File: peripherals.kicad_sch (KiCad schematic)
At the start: 14 parts, among them J2 GPS_ANT, U5 BME280, U6 LSM303AGR, U7 MAX-M10S, U8 RAK4630

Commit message: UPDATE RAK4630
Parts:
- added C39: 100n, symbol Device:C
- added C40: 10u, symbol Device:C
- added C41: 100N, symbol Device:C
- added J3: Conn_01x06, symbol Connector_Generic:Conn_01x06
- added J6: RF_LORA, symbol Connector:Conn_Coaxial
- added J7: BLE_ANT, symbol Connector:Conn_Coaxial
- added R25: 10K, symbol Device:R
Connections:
- net +3.3V: now also U8.40 (VBAT_IO_SX), U8.42 (VBAT_SX), C39.1, C40.1; no longer C35.2, C38.1, U5.6 (VDDIO), U6.10 (VDD_IO)
- net GND: now also U7.15 (VIO_SEL), U8.1 (GND), U8.2 (GND1), U8.3 (GND2), U8.4 (GND3), U8.5 (GND4), U8.6 (GND5), U8.7 (GND6), C39.2, C40.2, C41.2, J3.3 (Pin_3), J3.6 (Pin_6), J6.2 (Ext), J7.2 (Ext)
- net VSYS: now also U8.41 (VBAT_NRF)
- net at U8.34 (RF_BT): now also J7.1 (In)
- net at U8.35 (RF_LORA): now also J6.1 (In)
- net SWDCLK: now reaches U8.36 (SWDCLK)
- net SWDCLK: now also J3.4 (Pin_4)
- net SWDIO: now reaches U8.37 (SWDIO)
- net SWDIO: now also J3.2 (Pin_2)
- net VBUS: now reaches U8.43 (VBUS)
- net LORA_VDD: now reaches U8.44 (VDD_NRF)
- net LORA_VDD: now also J3.1 (Pin_1), R25.1
- net NRF_RST: now reaches U8.8 (NRF_RESET)
- net NRF_RST: now also C41.1, J3.5 (Pin_5), R25.2
- new net +1.8V: C35.2, C38.1, U5.6 (VDDIO), U6.10 (VDD_IO)
- no-connect marks 13 -> 12
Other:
- moved on the sheet: LoRa1, LoRa_PWR1, RCC1, U8, VSYS1

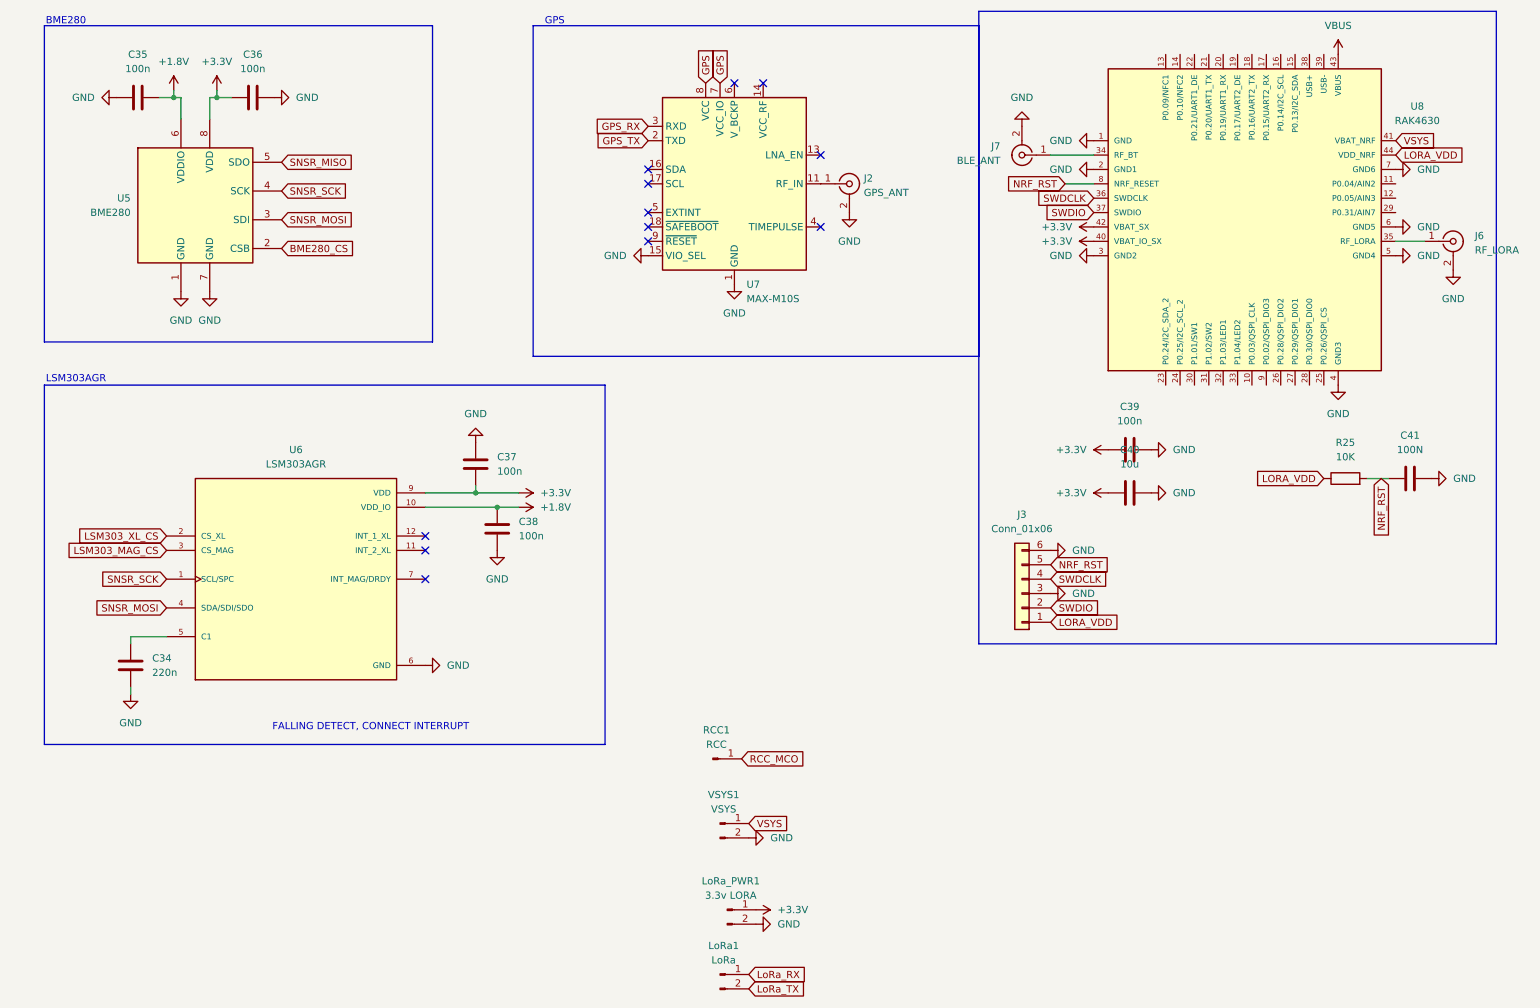
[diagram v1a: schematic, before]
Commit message: Modified lora module design, still need led and usb connected for flashing
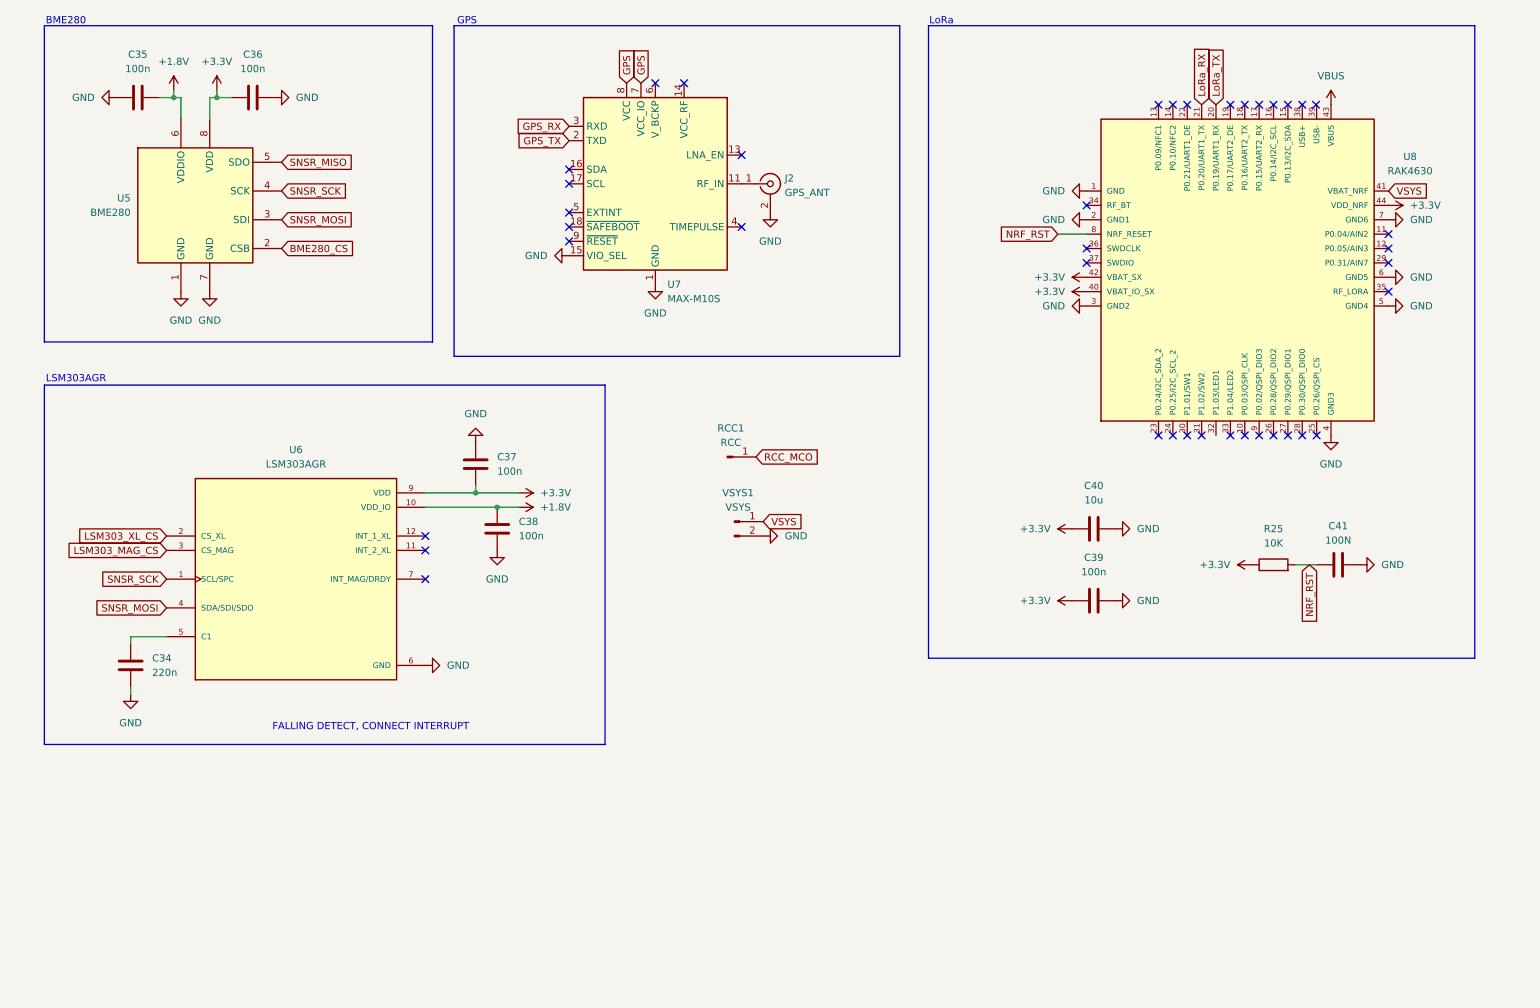
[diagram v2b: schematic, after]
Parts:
- removed J3: Conn_01x06, symbol Connector_Generic:Conn_01x06
- removed J6: RF_LORA, symbol Connector:Conn_Coaxial
- removed J7: BLE_ANT, symbol Connector:Conn_Coaxial
- removed LoRa1: LoRa, Connector_PinHeader_2.54mm:PinHeader_1x02_P2.54mm_Vertical, symbol Connector:Conn_01x02_Pin
- removed LoRa_PWR1: 3.3v LORA, Connector_PinHeader_2.54mm:PinHeader_1x02_P2.54mm_Vertical, symbol Connector:Conn_01x02_Pin
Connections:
- net LORA_VDD is gone; now on net +3.3V: R25.1, U8.44 (VDD_NRF)
- net LoRa_RX: now also U8.21 (P0.20/UART1_TX)
- net LoRa_TX: now also U8.20 (P0.19/UART1_RX)
- net SWDCLK: no longer names the net of U8.36 (SWDCLK)
- net SWDIO: no longer names the net of U8.37 (SWDIO)
- no-connect marks 12 -> 40
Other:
- note added: "LoRa"
- moved on the sheet: C39, C40, C41, J2, R25, RCC1, U7, U8, VSYS1

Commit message: Added logic level shifter for lora
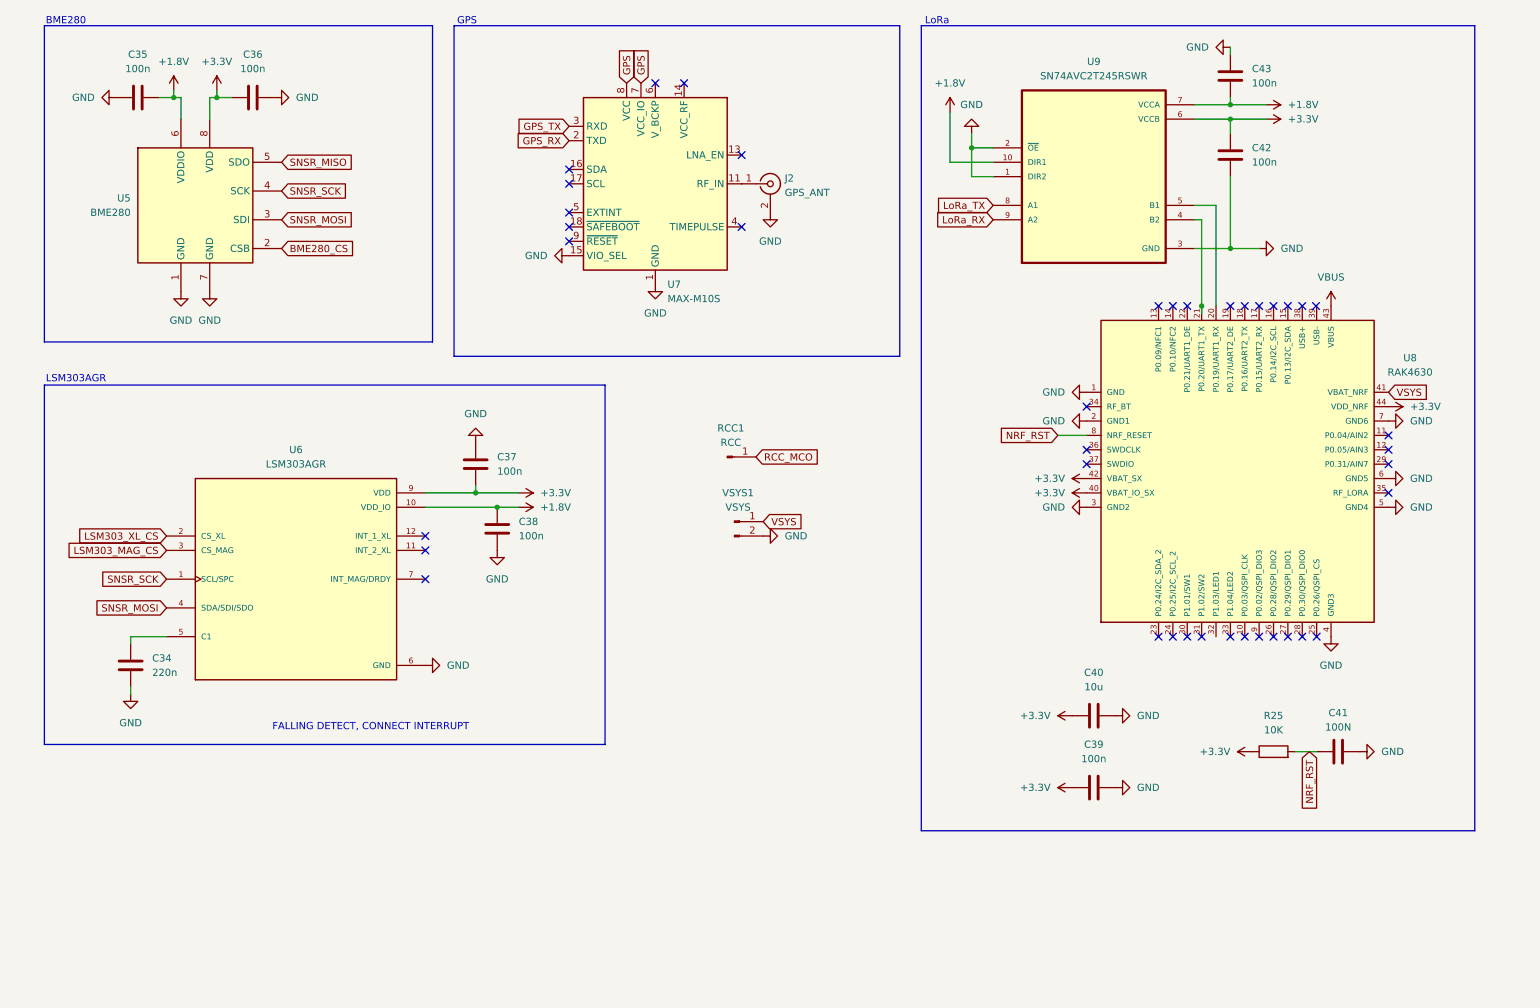
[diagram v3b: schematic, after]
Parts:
- added C42, C43: 100n, symbol Device:C
- added U9: SN74AVC2T245RSWR, SN74AVC2T245RSWR:QFN40P180X140X55-10N, symbol TheSummitProject:SN74AVC2T245RSWR
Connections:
- net +1.8V: now also C43.2, U9.10 (DIR1), U9.7 (VCCA)
- net +3.3V: now also C42.1, U9.6 (VCCB)
- net GND: now also C42.2, C43.1, U9.1 (DIR2), U9.2 (~{OE}), U9.3 (GND)
- net GPS_RX: now also U7.2 (TXD); no longer U7.3 (RXD)
- net GPS_TX: now also U7.3 (RXD); no longer U7.2 (TXD)
- net LoRa_RX: now also U9.9 (A2); no longer U8.21 (P0.20/UART1_TX)
- net LoRa_TX: now also U9.8 (A1); no longer U8.20 (P0.19/UART1_RX)
- new net: U8.20 (P0.19/UART1_RX), U9.5 (B1)
- new net: U8.21 (P0.20/UART1_TX), U9.4 (B2)
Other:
- moved on the sheet: C39, C40, C41, R25, U8

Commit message: added mux for usb, cleaned up schematic for pcb design, setup new pcb with correct size
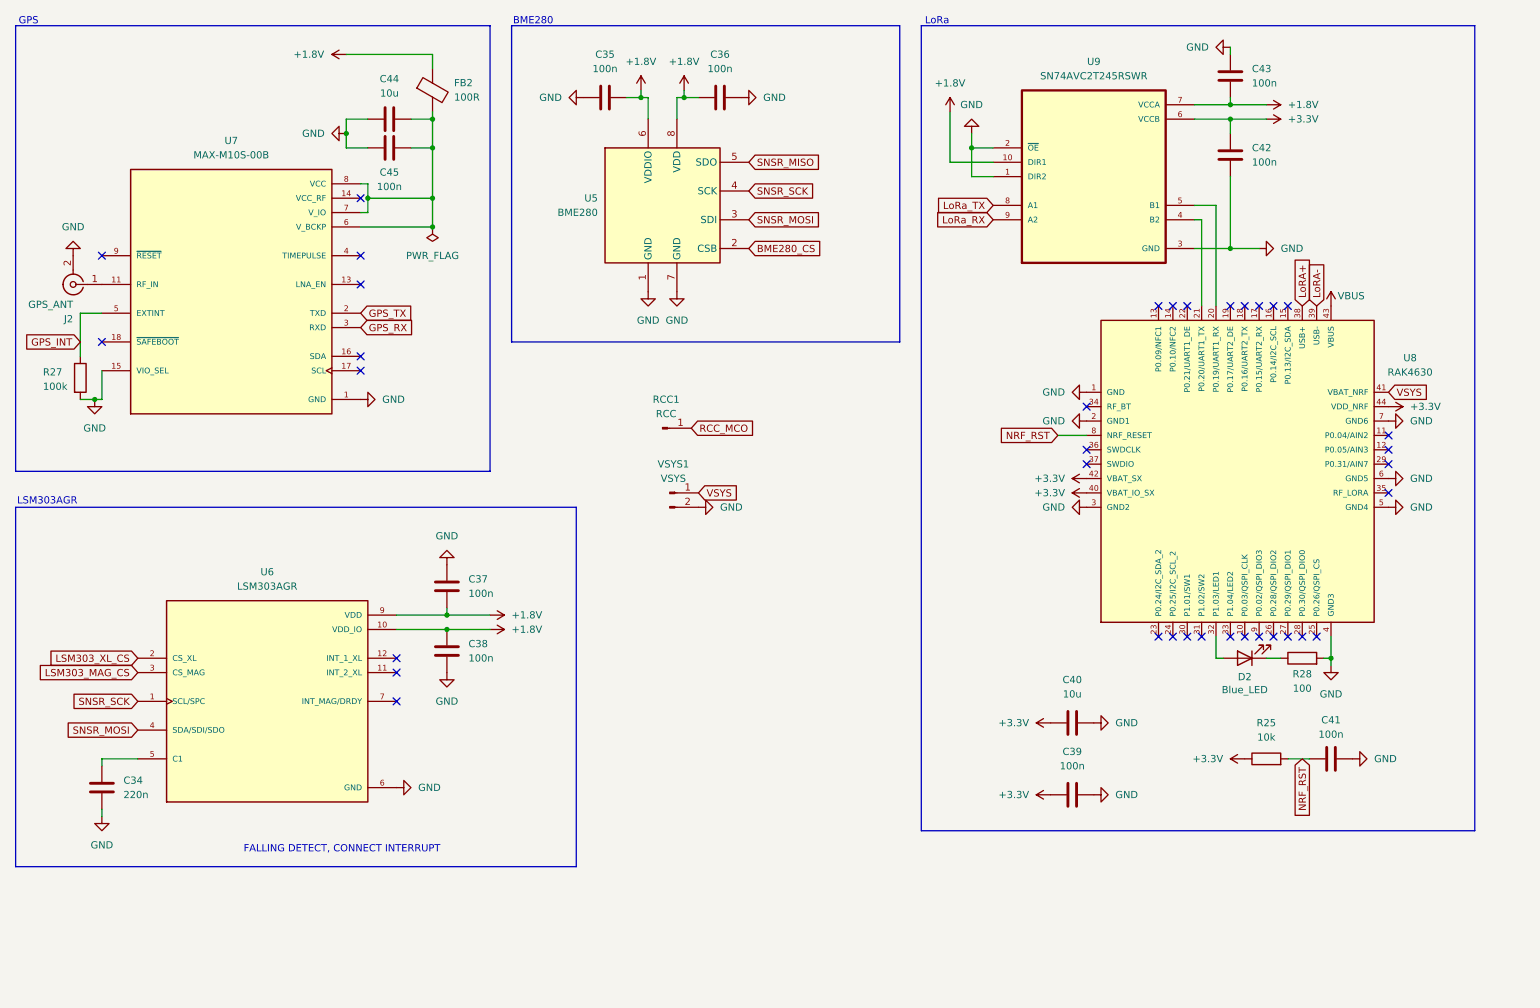
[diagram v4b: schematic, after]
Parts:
- removed U7: MAX-M10S, RF_GPS:ublox_MAX, symbol RF_GPS:MAX-M10S
- added C44: 10u, Capacitor_SMD:C_0805_2012Metric, symbol Device:C
- added C45: 100n, Capacitor_SMD:C_0603_1608Metric, symbol Device:C
- added D2: Blue_LED, LED_SMD:LED_1206_3216Metric, symbol Device:LED
- added FB2: 100R, Inductor_SMD:L_0603_1608Metric, symbol Device:FerriteBead
- added R27: 100k, Resistor_SMD:R_0603_1608Metric, symbol Device:R
- added R28: 100, Resistor_SMD:R_0603_1608Metric, symbol Device:R
- added U7: MAX-M10S-00B, TheSummitProject:XCVR_MAX-M10S-00B, symbol TheSummitProject:MAX-M10S-00B
- C34, C35, C36, C37, C38, C39, C42, C43: footprint (none) -> Capacitor_SMD:C_0603_1608Metric
- C40: footprint (none) -> Capacitor_SMD:C_0805_2012Metric
- C41: value 100N -> 100n; footprint (none) -> Capacitor_SMD:C_0603_1608Metric
- J2: footprint (none) -> RF_Antenna:Antenova_SR4G013_GPS
- R25: value 10K -> 10k; footprint (none) -> Resistor_SMD:R_0603_1608Metric
- RCC1: footprint TestPoint:TestPoint_Pad_D1.5mm -> TestPoint:TestPoint_Pad_D1.0mm
- U6: footprint LSM303AGR:PQFN50P200X200X100-12N -> TheSummitProject:PQFN50P200X200X100-12N
- U8: footprint RAK4630:RAK4630 -> TheSummitProject:RAK4630
- U9: footprint SN74AVC2T245RSWR:QFN40P180X140X55-10N -> TheSummitProject:QFN40P180X140X55-10N
- VSYS1: footprint Connector_PinHeader_2.54mm:PinHeader_1x02_P2.54mm_Vertical -> TestPoint:TestPoint_2Pads_Pitch2.54mm_Drill0.8mm
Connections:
- net +1.8V: now also C36.1, C37.2, U5.8 (VDD), U6.9 (VDD), FB2.1
- net +3.3V: no longer C36.1, C37.2, U5.8 (VDD), U6.9 (VDD)
- net GND: now also C44.1, C45.2, R27.2, R28.2, U7.1 (GND), U7.10 (GND), U7.12 (GND), U7.15 (VIO_SEL)
- net GPS_RX: now also U7.3 (RXD)
- net GPS_TX: now also U7.2 (TXD)
- net at U8.32 (P1.03/LED1): now also D2.2 (A)
- net LoRA+: now reaches U8.38 (USB+)
- net LoRA-: now reaches U8.39 (USB-)
- net at J2.1 (In): now also U7.11 (RF_IN)
- new net: C44.2, C45.1, FB2.2, U7.6 (V_BCKP), U7.7 (V_IO), U7.8 (VCC)
- new net: D2.1 (K), R28.1
- new net GPS_INT: R27.1, U7.5 (EXTINT)
- no-connect marks 40 -> 36
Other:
- moved on the sheet: C34, C37, C38, C39, C40, C41, R25, RCC1, U6, VSYS1

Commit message: changed FB2 to 120R to consilidate BOM
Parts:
- FB2: value 100R -> 120R
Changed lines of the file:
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@@
 			)
 		)
-		(property "Value" "100R"
+		(property "Value" "120R"
 			(at 97.79 32.9691 0)
 			(show_name no)
